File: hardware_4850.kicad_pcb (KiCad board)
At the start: 2 copper layers, 282 parts, among them J101 PWM, J102 ADC, J103 PWM, J104 ADC, J105 +, J106 A, J107 B, J108 C, J109 GND, J1101 HALL, J1102 Enable, J1103 CAN_IN, J1104 CAN_Out, J601 AIN, J602 USB_B_Mini, J701 MOT_TEMP, P1101 SWD, Q201 NCEP6080AG, Q202 NCEP6080AG, Q203 NCEP6080AG, Q204 NCEP6080AG, Q301 NCEP6080AG, Q302 NCEP6080AG, Q303 NCEP6080AG, Q304 NCEP6080AG, Q401 NCEP6080AG, Q402 NCEP6080AG, Q403 NCEP6080AG, Q404 NCEP6080AG, U1001 GS8632-MR, U1101 TCAN334, U1102 24LC04, U201 LM5109BMA, U202 INA240A1PWR, U301 LM5109BMA, U302 INA240A1PWR, U401 LM5109BMA, U402 INA240A1PWR, U501 LMR12010Y, U502 LM5008, U601 STM32F730R8Tx, U701 GS8632-MR, U801 GS8632-MR, U901 GS8632-MR, X601 SM44T

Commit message: added enclosure
- first placing of power stage finished
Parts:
- removed C206, C208, C306, C308, C406, C408: 100u, Capacitor_SMD:CP_Elec_8x11.9
- removed R201, R202, R301, R302, R401, R402: 1R1, Resistor_SMD:R_0603_1608Metric
- added C1106: 1u, Capacitor_SMD:C_0603_1608Metric, F.Cu at (451.3, 56.7)
- added C1107: 1u, Capacitor_SMD:C_0603_1608Metric, F.Cu at (443.0, 65.6)
- added N101: Housing_Pad, hardware_4850:RND-455-00370, F.Cu at (47.2, 15.2)
- added N101: Housing_Pad, hardware_4850:RND-455-00370, F.Cu at (47.3, 103.5)
- added R606: 1R1, Resistor_SMD:R_0603_1608Metric, F.Cu at (371.5, -0.50)
- added R607: 1R1, Resistor_SMD:R_0603_1608Metric, F.Cu at (371.5, 2.01)
- added R608: 1R1, Resistor_SMD:R_0603_1608Metric, F.Cu at (375.5, -0.50)
- added R609: 1R1, Resistor_SMD:R_0603_1608Metric, F.Cu at (375.5, 2.01)
- added R610: 1R1, Resistor_SMD:R_0603_1608Metric, F.Cu at (379.5, -0.50)
- added R611: 1R1, Resistor_SMD:R_0603_1608Metric, F.Cu at (379.5, 2.01)
- added U1103: AP2204K-5.0, Package_TO_SOT_SMD:SOT-23-5, F.Cu at (408.6, 72.1)
- C204, C304, C404, C501: value 1u -> 10u
- C207, C209, C307, C309, C407, C409: value 100u -> 56u; footprint Capacitor_SMD:CP_Elec_8x11.9 -> Capacitor_SMD:CP_Elec_10x10
- moved C802 328.3 mm to (424.2, 83.8)
- moved C804 328.3 mm to (424.2, 86.3)
- moved C805 324.2 mm to (424.2, 88.8)
- moved C807 320.3 mm to (424.2, 81.3)
- moved R806 320.2 mm to (412.1, 86.0)
- moved C803 320.2 mm to (420.2, 88.8)
- moved R603 319.2 mm to (458.8, 19.9)
- moved C801 316.8 mm to (420.2, 86.3)
- moved R802 316.3 mm to (408.1, 86.0)
- moved C808 316.3 mm to (416.2, 86.3)
- moved C809 316.3 mm to (420.2, 83.8)
- moved C810 316.3 mm to (416.2, 88.8)
- moved U801 316.3 mm to (409.9, 79.9)
- moved R801 316.3 mm to (415.6, 78.8)
- moved R803 316.3 mm to (412.1, 83.5)
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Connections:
- C201 pad 2: GNDPWR -> Net-(C201-Pad2)
- C202 pad 2: GNDPWR -> Net-(C201-Pad2)
- C207 pad 1: Net-(C206-Pad2) -> +BATT
- C209 pad 1: Net-(C208-Pad2) -> +BATT
- C301 pad 2: GNDPWR -> Net-(C301-Pad2)
- C302 pad 2: GNDPWR -> Net-(C301-Pad2)
- C307 pad 1: Net-(C306-Pad2) -> +BATT
- C309 pad 1: Net-(C308-Pad2) -> +BATT
- C401 pad 2: GNDPWR -> Net-(C401-Pad2)
- C402 pad 2: GNDPWR -> Net-(C401-Pad2)
- C407 pad 1: Net-(C406-Pad2) -> +BATT
- C409 pad 1: Net-(C408-Pad2) -> +BATT
- J1101 pad 1: +3V3 -> Net-(C1106-Pad1)
- R203 pad 2: Net-(R203-Pad2) -> Net-(C203-Pad2)
- R206 pad 2: GNDPWR -> Net-(C201-Pad2)
- R208 pad 2: GNDPWR -> Net-(C201-Pad2)
- R209 pad 2: Net-(R203-Pad2) -> Net-(C203-Pad2)
- R303 pad 2: Net-(R303-Pad2) -> Net-(C303-Pad2)
- R306 pad 2: GNDPWR -> Net-(C301-Pad2)
- R308 pad 2: GNDPWR -> Net-(C301-Pad2)
- R309 pad 2: Net-(R303-Pad2) -> Net-(C303-Pad2)
- R403 pad 2: Net-(R403-Pad2) -> Net-(C403-Pad2)
- R406 pad 2: GNDPWR -> Net-(C401-Pad2)
- R408 pad 2: GNDPWR -> Net-(C401-Pad2)
- R409 pad 2: Net-(R403-Pad2) -> Net-(C403-Pad2)
- U201 pad 2: Net-(R201-Pad1) -> /phase_a/PwmH
- U201 pad 3: Net-(R202-Pad1) -> /phase_a/PwmL
- U201 pad 4: GNDPWR -> Net-(C201-Pad2)
- U201 pad 7: Net-(R203-Pad2) -> Net-(C203-Pad2)
- U301 pad 2: Net-(R301-Pad1) -> /phase_b/PwmH
- U301 pad 3: Net-(R302-Pad1) -> /phase_b/PwmL
- U301 pad 4: GNDPWR -> Net-(C301-Pad2)
- U301 pad 7: Net-(R303-Pad2) -> Net-(C303-Pad2)
- U401 pad 2: Net-(R401-Pad1) -> /phase_c/PwmH
- U401 pad 3: Net-(R402-Pad1) -> /phase_c/PwmL
- U401 pad 4: GNDPWR -> Net-(C401-Pad2)
- U401 pad 7: Net-(R403-Pad2) -> Net-(C403-Pad2)
- U601 pad 34: /controller/PwmAL -> Net-(R606-Pad2)
- U601 pad 35: /controller/PwmBL -> Net-(R607-Pad2)
- U601 pad 36: /controller/PwmCL -> Net-(R608-Pad2)
- U601 pad 41: /controller/PwmAH -> Net-(R609-Pad2)
- U601 pad 42: /controller/PwmBH -> Net-(R610-Pad2)
- U601 pad 43: /controller/PwmCH -> Net-(R611-Pad2)
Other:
- board outline added: 84 x 167.2 mm

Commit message: started placing of logic board
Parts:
- removed H101, H105, H106, H107, H108: MountingHole_Pad, MountingHole:MountingHole_4.3mm_M4_ISO14580_Pad
- removed H102, H103, H104: MountingHole, MountingHole:MountingHole_3.2mm_M3_ISO14580
- added D505: SS110R3G, Diode_SMD:D_SMA, F.Cu at (260.5, 137.2)
- C505, C509, C601, C603, C606, C612, J101, J102, R501, R502, R505, R506, R604, R605, R606, R607, R608, R609, R610, R611, X601: moved to B.Cu
- moved R603 389.2 mm to (71.5, 58.0)
- moved R602 387.6 mm to (71.5, 60.8)
- moved R601 386.3 mm to (67.5, 80.8), turned to 180 degrees
- moved R604 385.7 mm to (70.0, 68.5), turned to 270 degrees
- moved R605 384.5 mm to (71.5, 68.5), turned to 90 degrees
- moved J602 378.8 mm to (63.5, 72.2), turned to 270 degrees
- moved J601 371.1 mm to (67.8, 63.2), turned to 180 degrees
- moved R1101 368.0 mm to (71.5, 48.5)
- moved JP601 366.2 mm to (63.0, 80.8), turned to 180 degrees
- moved C610 365.4 mm to (91.8, 60.8), turned to 90 degrees
- moved C609 360.4 mm to (96.0, 50.8)
- moved R1113 355.3 mm to (94.2, 73.8)
- moved D1102 353.6 mm to (95.5, 38.8), turned to 270 degrees
- moved R1106 353.5 mm to (94.0, 42.0), turned to 270 degrees
- moved C605 352.7 mm to (108.2, 56.5), turned to 270 degrees
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
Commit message: more logic placing, switched halls for better routing
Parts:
- moved R1105 258.6 mm to (194.8, 95.5)
- moved R714 152.8 mm to (207.5, 94.2), turned to 270 degrees
- moved C1105 147.5 mm to (236.5, 135.5)
- moved JP1101 147.5 mm to (230.8, 133.8)
- moved R1112 147.5 mm to (230.5, 128.8)
- moved R1113 147.5 mm to (230.5, 130.2)
- moved R1115 147.5 mm to (230.5, 131.8)
- moved U1102 147.5 mm to (236.8, 130.8)
- moved R712 147.3 mm to (217.0, 93.2), turned to 270 degrees
- moved R709 144.7 mm to (219.8, 88.2)
- moved R710 144.5 mm to (212.5, 93.2), turned to 270 degrees
- moved R711 142.9 mm to (214.0, 93.2), turned to 90 degrees
- moved R705 142.6 mm to (219.8, 85.2), turned to 180 degrees
- moved C702 141.7 mm to (216.5, 85.2)
- moved R713 140.8 mm to (215.5, 93.2), turned to 90 degrees
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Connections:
- U601 pad 2: /controller/interfaces/HallA -> /controller/interfaces/HallC
- U601 pad 4: /controller/interfaces/HallC -> /controller/interfaces/HallA
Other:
- board size 84 x 167.2 mm -> 207.2 x 123 mm

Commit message: finished placing :)
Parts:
- removed the N101 at (170.5, 59.5)
- added C711: 100n, Capacitor_SMD:C_0603_1608Metric, B.Cu at (205.8, 90.8)
- added C712: 100n, Capacitor_SMD:C_0603_1608Metric, B.Cu at (205.8, 92.2)
- added N102: Housing_Pad, hardware_4850:RND-455-00370, F.Cu at (170.5, 59.5)
- C1006, C1007, C1010, C512, C710, C806, C807, C810, C906, C907, C910, FB501, FB502, R716: moved to B.Cu
- J1101: footprint Connector_PinHeader_2.54mm:PinHeader_1x05_P2.54mm_Horizontal -> Connector_JST:JST_PH_S5B-PH-K_1x05_P2.00mm_Horizontal
- J1102, J701: footprint Connector_PinHeader_2.54mm:PinHeader_1x02_P2.54mm_Horizontal -> Connector_JST:JST_PH_S2B-PH-K_1x02_P2.00mm_Horizontal
- J1103, J1104, J601: footprint Connector_PinHeader_2.54mm:PinHeader_1x04_P2.54mm_Horizontal -> Connector_JST:JST_PH_S4B-PH-K_1x04_P2.00mm_Horizontal
- moved C1001 186.1 mm to (229.0, 94.5), turned to 90 degrees
- moved R810 185.9 mm to (241.5, 116.0), turned to 90 degrees
- moved C1002 185.0 mm to (230.5, 84.0), turned to 90 degrees
- moved R1008 184.9 mm to (229.5, 91.2)
- moved R1009 181.9 mm to (229.5, 89.8), turned to 180 degrees
- moved C805 181.7 mm to (244.5, 116.0), turned to 90 degrees
- moved C1006 181.7 mm to (229.5, 88.2)
- moved C802 179.6 mm to (247.5, 116.0), turned to 270 degrees
- moved C804 179.2 mm to (246.0, 105.5), turned to 90 degrees
- moved C1004 179.0 mm to (232.0, 94.5), turned to 270 degrees
- moved R1004 178.7 mm to (232.0, 84.0), turned to 90 degrees
- moved R1011 178.6 mm to (236.5, 94.5), turned to 90 degrees
- moved C807 178.0 mm to (248.5, 110.0), turned to 180 degrees
- moved C803 178.0 mm to (243.0, 105.5), turned to 90 degrees
- moved R1007 177.8 mm to (229.5, 88.2), turned to 180 degrees
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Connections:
- C1008 pad 2: /controller/AIN_CUR_C -> /controller/analog/IcDC
- C1009 pad 2: /controller/AIN_CUR_C_AC -> /controller/analog/IcAC
- C1101 pad 1: /controller/interfaces/HallC -> /controller/interfaces/HallA
- C1103 pad 1: /controller/interfaces/HallA -> /controller/interfaces/HallC
- C808 pad 2: /controller/analog/IaDC -> /controller/AIN_CUR_A
- C809 pad 2: /controller/analog/IaAC -> /controller/AIN_CUR_A_AC
- J1101 pad 1: Net-(C1106-Pad1) -> GNDD
- J1101 pad 5: GNDD -> Net-(C1106-Pad1)
- J601 pad 1: +3.3VADC -> GNDA
- J601 pad 4: GNDA -> +3.3VADC
- R1010 pad 1: /controller/AIN_CUR_C -> /controller/analog/IcDC
- R1011 pad 1: /controller/AIN_CUR_C_AC -> /controller/analog/IcAC
- R1102 pad 1: /controller/interfaces/HallA -> /controller/interfaces/HallC
- R1102 pad 2: Net-(J1101-Pad2) -> Net-(J1101-Pad4)
- R1104 pad 1: /controller/interfaces/HallC -> /controller/interfaces/HallA
- R1104 pad 2: Net-(J1101-Pad4) -> Net-(J1101-Pad2)
- R1114 pad 1: Net-(J1103-Pad4) -> Net-(J1103-Pad1)
- R602 pad 1: Net-(J601-Pad2) -> Net-(J601-Pad3)
- R603 pad 1: Net-(J601-Pad3) -> Net-(J601-Pad2)
- R810 pad 1: /controller/analog/IaDC -> /controller/AIN_CUR_A
- R811 pad 1: /controller/analog/IaAC -> /controller/AIN_CUR_A_AC
- U1101 pad 6: Net-(J1103-Pad3) -> Net-(J1103-Pad2)
- U1101 pad 7: Net-(J1103-Pad2) -> Net-(J1103-Pad3)
- U601 pad 10: /controller/AIN_CUR_C -> /controller/AIN_CUR_A
- U601 pad 11: /controller/AIN_CUR_C_AC -> /controller/AIN_CUR_A_AC
- U601 pad 16: /controller/analog/IaDC -> /controller/analog/IcDC
- U601 pad 17: /controller/analog/IaAC -> /controller/analog/IcAC
- U601 pad 2: /controller/interfaces/HallC -> /controller/interfaces/HallA
- U601 pad 4: /controller/interfaces/HallA -> /controller/interfaces/HallC

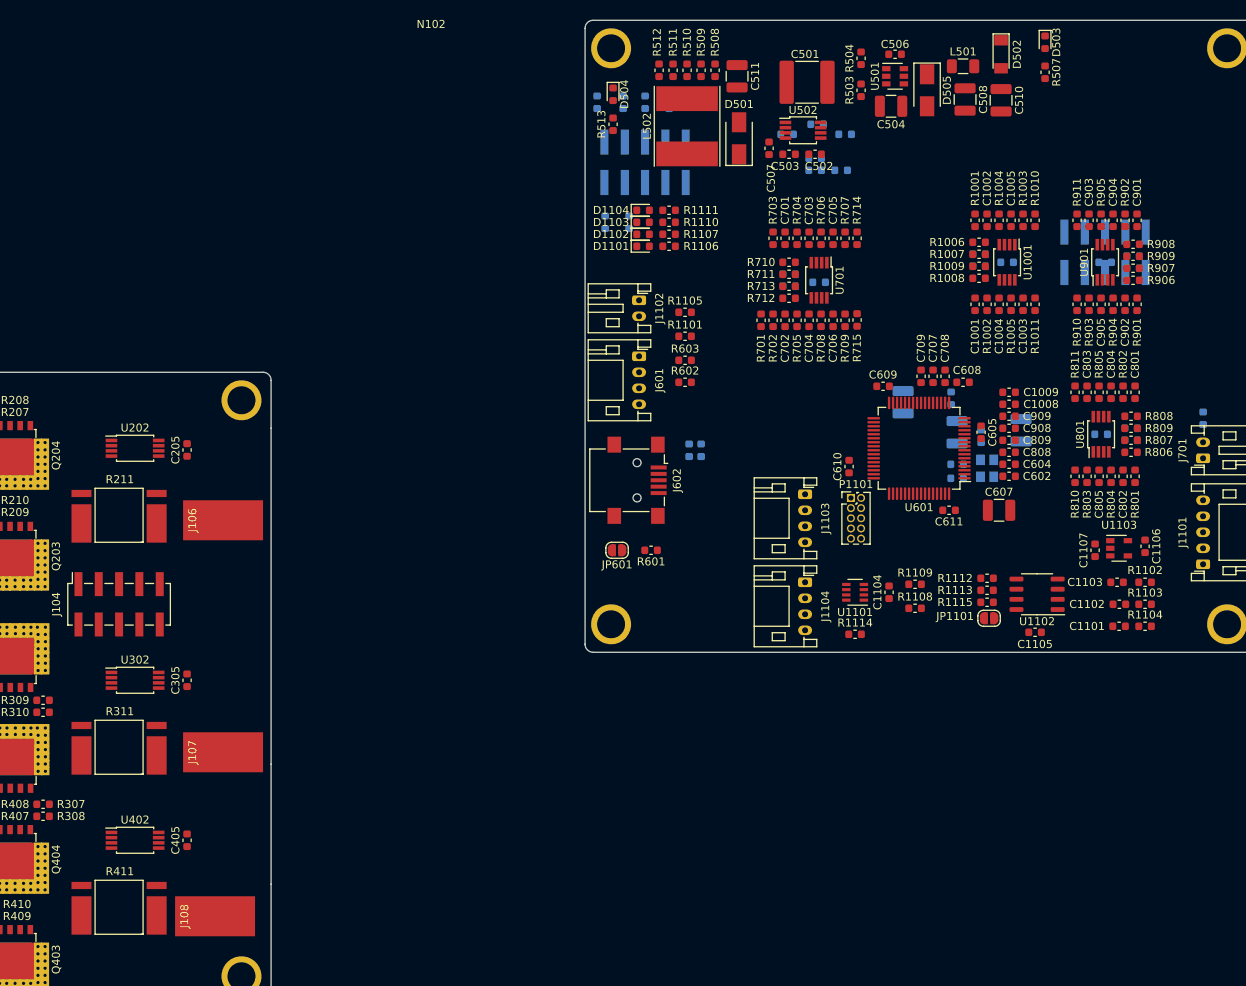
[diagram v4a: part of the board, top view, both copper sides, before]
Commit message: changed shunts to standard footprint for more alternatives
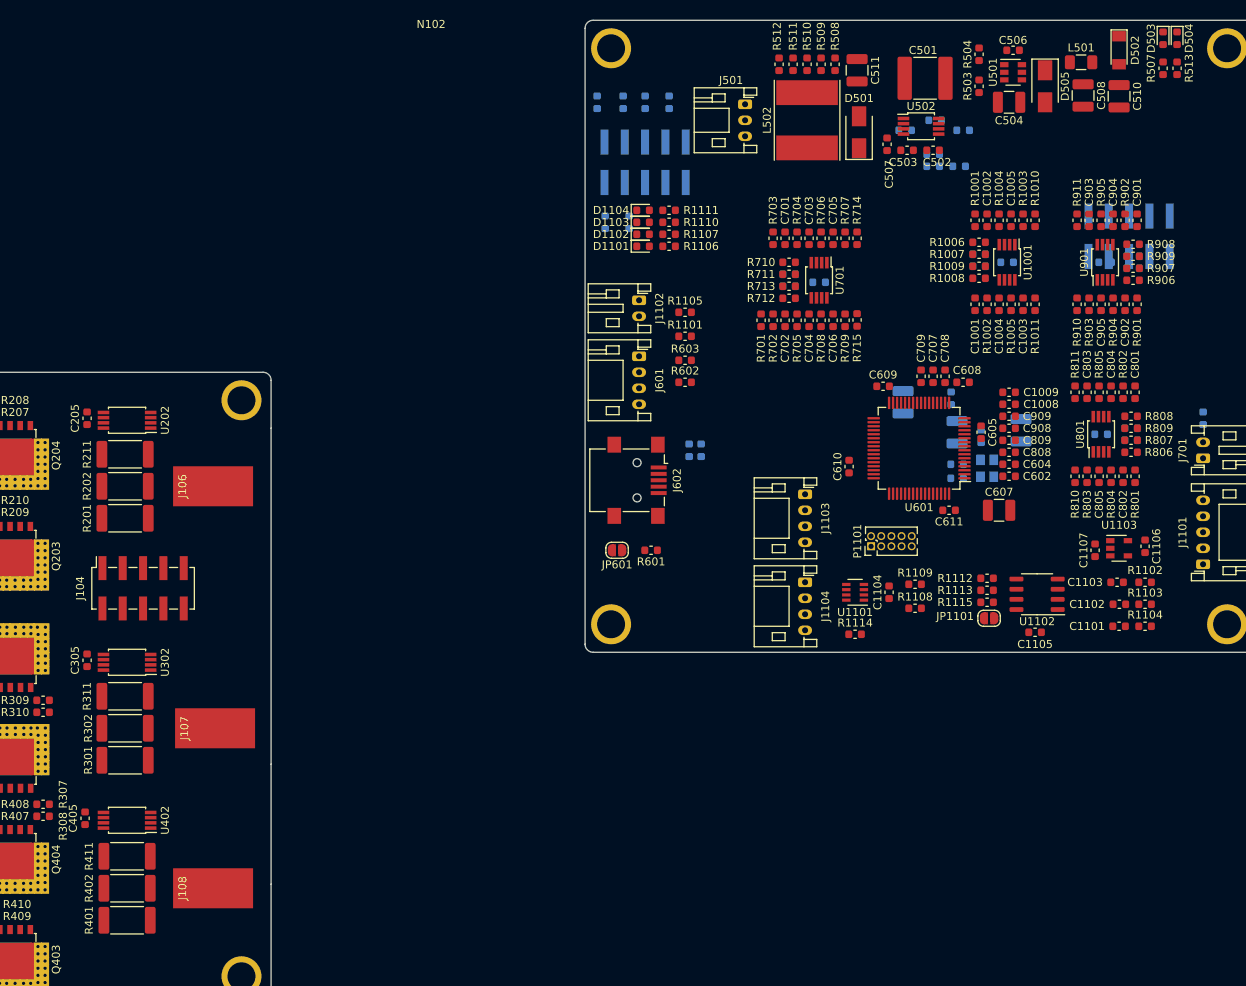
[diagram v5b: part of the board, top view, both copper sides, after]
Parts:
- added J501: Enable, Connector_JST:JST_PH_S3B-PH-K_1x03_P2.00mm_Horizontal, F.Cu at (200.2, 69.5)
- added R201: 2mR, Resistor_SMD:R_2512_6332Metric, F.Cu at (122.8, 121.2)
- added R202: 2mR, Resistor_SMD:R_2512_6332Metric, F.Cu at (122.8, 117.2)
- added R301: 2mR, Resistor_SMD:R_2512_6332Metric, F.Cu at (122.8, 151.5)
- added R302: 2mR, Resistor_SMD:R_2512_6332Metric, F.Cu at (122.8, 147.5)
- added R401: 2mR, Resistor_SMD:R_2512_6332Metric, F.Cu at (123.0, 171.5)
- added R402: 2mR, Resistor_SMD:R_2512_6332Metric, F.Cu at (123.0, 167.5)
- J1102: value Enable -> PWM_EN
- R211, R311, R411: value 1mR -> 2mR; footprint hardware_4850:KWSL_4_Terminal_Shunt -> Resistor_SMD:R_2512_6332Metric
- moved D504 70.8 mm to (254.2, 61.2)
- moved R513 70.8 mm to (254.2, 65.0)
- moved C511 15.0 mm to (214.2, 65.2)
- moved D501 15.0 mm to (214.5, 73.0)
- moved L502 15.0 mm to (208.0, 71.5)
- moved R508 15.0 mm to (211.5, 64.5)
- moved R509 15.0 mm to (209.8, 64.5)
- moved R510 15.0 mm to (208.0, 64.5)
- moved R511 15.0 mm to (206.2, 64.5)
- moved R512 15.0 mm to (204.5, 64.5)
- moved C501 14.8 mm to (222.8, 66.2)
- moved C502 14.8 mm to (223.8, 75.2)
- moved C503 14.8 mm to (220.5, 75.2)
- moved C504 14.8 mm to (233.2, 69.2)
- moved C505 14.8 mm to (224.0, 71.5)
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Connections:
- C501 pad 1: +48V -> Net-(C501-Pad1)
- C502 pad 1: +48V -> Net-(C501-Pad1)
- R211 pad 2: Net-(R211-Pad2) -> Net-(Q201-Pad1)
- R311 pad 2: Net-(R311-Pad2) -> Net-(Q301-Pad1)
- R411 pad 2: Net-(R411-Pad2) -> Net-(Q401-Pad1)
- R501 pad 2: +48V -> Net-(C501-Pad1)
- U202 pad 2: Net-(R211-Pad2) -> /phase_a/Phase
- U202 pad 3: Net-(R211-Pad3) -> Net-(Q201-Pad1)
- U302 pad 2: Net-(R311-Pad2) -> /phase_b/Phase
- U302 pad 3: Net-(R311-Pad3) -> Net-(Q301-Pad1)
- U402 pad 2: Net-(R411-Pad2) -> /phase_c/Phase
- U402 pad 3: Net-(R411-Pad3) -> Net-(Q401-Pad1)
- U502 pad 8: +48V -> Net-(C501-Pad1)

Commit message: started routing of power stage
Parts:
- moved C303 2.85 mm to (71.2, 152.2)
- moved C403 2.85 mm to (71.2, 165.3)
- moved U401 2.85 mm to (66.0, 165.8)
- moved C201 2.76 mm to (61.2, 113.2)
- moved D301 2.47 mm to (66.0, 148.0)
- moved C402 2.37 mm to (61.2, 165.8)
- moved C401 2.16 mm to (59.2, 165.8)
- moved D401 2.15 mm to (66.0, 161.0)
- moved U201 1.82 mm to (68.0, 111.2)
- moved U301 1.82 mm to (66.0, 152.8)
- moved C202 1.58 mm to (63.2, 112.5)
- moved C302 0.79 mm to (61.2, 152.8)
- moved D201 0.71 mm to (68.0, 106.5)
- moved C301 0.56 mm to (59.2, 152.8)
- moved Q304 0.25 mm to (109.0, 152.4)
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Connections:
- R203 pad 2: Net-(C203-Pad2) -> Net-(R203-Pad2)
- R209 pad 2: Net-(C203-Pad2) -> Net-(R203-Pad2)
- R303 pad 2: Net-(C303-Pad2) -> Net-(R303-Pad2)
- R309 pad 2: Net-(C303-Pad2) -> Net-(R303-Pad2)
- R403 pad 2: Net-(C403-Pad2) -> Net-(R403-Pad2)
- R409 pad 2: Net-(C403-Pad2) -> Net-(R403-Pad2)
- U201 pad 7: Net-(C203-Pad2) -> Net-(R203-Pad2)
- U301 pad 7: Net-(C303-Pad2) -> Net-(R303-Pad2)
- U401 pad 7: Net-(C403-Pad2) -> Net-(R403-Pad2)
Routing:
- net GND: track 0.00 -> 135.0 mm, vias 0 -> 4
- net +3.3VA: track 0.00 -> 79.4 mm, vias 0 -> 4
- net Net-(C201-Pad2): track 0.00 -> 52.0 mm, vias 0 -> 3
- net Net-(R205-Pad2): track 0.00 -> 40.4 mm, vias 0 -> 3
- net Net-(J104-Pad10): track 0.00 -> 35.6 mm, vias 0 -> 2
- net +12P: track 0.00 -> 32.8 mm
- net Net-(J104-Pad8): track 0.00 -> 30.9 mm, vias 0 -> 2
- net /phase_c/I: track 0.00 -> 30.8 mm, vias 0 -> 2
- net Net-(R203-Pad2): track 0.00 -> 30.0 mm, vias 0 -> 3
- net Net-(C203-Pad2): track 0.00 -> 25.2 mm, vias 0 -> 3
- net /phase_a/I: track 0.00 -> 25.0 mm, vias 0 -> 2
- net /phase_b/I: track 0.00 -> 20.2 mm, vias 0 -> 2
- net Net-(Q401-Pad1): track 0.00 -> 14.0 mm, vias 0 -> 52
- net Net-(Q301-Pad1): track 0.00 -> 13.8 mm, vias 0 -> 52
- net Net-(Q201-Pad1): track 0.00 -> 13.6 mm, vias 0 -> 52
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- added copper zone on B.Cu, net +BATT
- added copper zone on F.Cu, net +BATT
- added copper zone on GND, net +BATT
- added copper zone on B.Cu, net /phase_a/Phase
- added copper zone on F.Cu, net /phase_a/Phase
- added copper zone on B.Cu, net /phase_b/Phase
- added copper zone on F.Cu, net /phase_b/Phase
- added copper zone on B.Cu, net /phase_c/Phase
- added copper zone on F.Cu, net /phase_c/Phase
- added copper zone on B.Cu, net GNDPWR
- added copper zone on F.Cu, net GNDPWR
- added copper zone on GND, net GNDPWR
- added copper zone on B.Cu, net Net-(Q201-Pad1)
- added copper zone on F.Cu, net Net-(Q201-Pad1)
- added copper zone on B.Cu, net Net-(Q301-Pad1)
- added copper zone on F.Cu, net Net-(Q301-Pad1)
- added copper zone on B.Cu, net Net-(Q401-Pad1)
- added copper zone on F.Cu, net Net-(Q401-Pad1)
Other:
- copper layers 2 -> 4
- net class GateDrive added: clearance 0.2, trace_width 0.5, via_dia 0.8, via_drill 0.4
